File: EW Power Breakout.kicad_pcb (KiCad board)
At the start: 2 copper layers, 46.2 x 38.1 mm, 15 parts, among them J1 CONN_02X08, J2 JACK_2P, J3 JACK_2P, J4 JACK_2P, J5 JACK_2P, J6 CONN_01X14, U1 LM7805

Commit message: Fixed IDC routing bug
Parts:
- moved J6 2.51 mm to (157.0, 109.2)
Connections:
- D1 pad 2: Net-(D1-Pad2) -> /+12VI
- D2 pad 1: Net-(D2-Pad1) -> /-12VI
- J1 pad 1: Net-(J1-Pad1) -> /-12VI
- J1 pad 10: GND -> /+12VI
- J1 pad 12: GND -> Net-(J1-Pad12)
- J1 pad 13: Net-(J1-Pad13) -> /CV
- J1 pad 14: GND -> /CV
- J1 pad 15: Net-(J1-Pad15) -> /GATE
- J1 pad 16: Net-(D2-Pad1) -> /GATE
- J1 pad 2: /GATE -> /-12VI
- J1 pad 3: Net-(J1-Pad3) -> GND
- J1 pad 4: /CV -> GND
- J1 pad 5: Net-(J1-Pad5) -> GND
- J1 pad 6: Net-(J1-Pad6) -> GND
- J1 pad 7: Net-(J1-Pad7) -> GND
- J1 pad 8: Net-(D1-Pad2) -> GND
- J1 pad 9: Net-(J1-Pad9) -> /+12VI
- U1 pad 1: (no net) -> /+12V
- U1 pad 2: (no net) -> GND
- U1 pad 3: (no net) -> /+5V
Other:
- board size 46.2 x 38.1 mm -> 48.3 x 38.1 mm
- board text added: "+12V"
- board text added: "+5V"
- board text added: "-12V"
- board text added: "CV"
- board text added: "GATE"
- board text added: "GND"
- board text added: "J1"
- board text added: "J1SW"
- board text added: "J2"
- board text added: "J2SW"
- board text added: "J3"
- board text added: "J3SW"
- board text added: "J4"
- board text added: "J4SW"

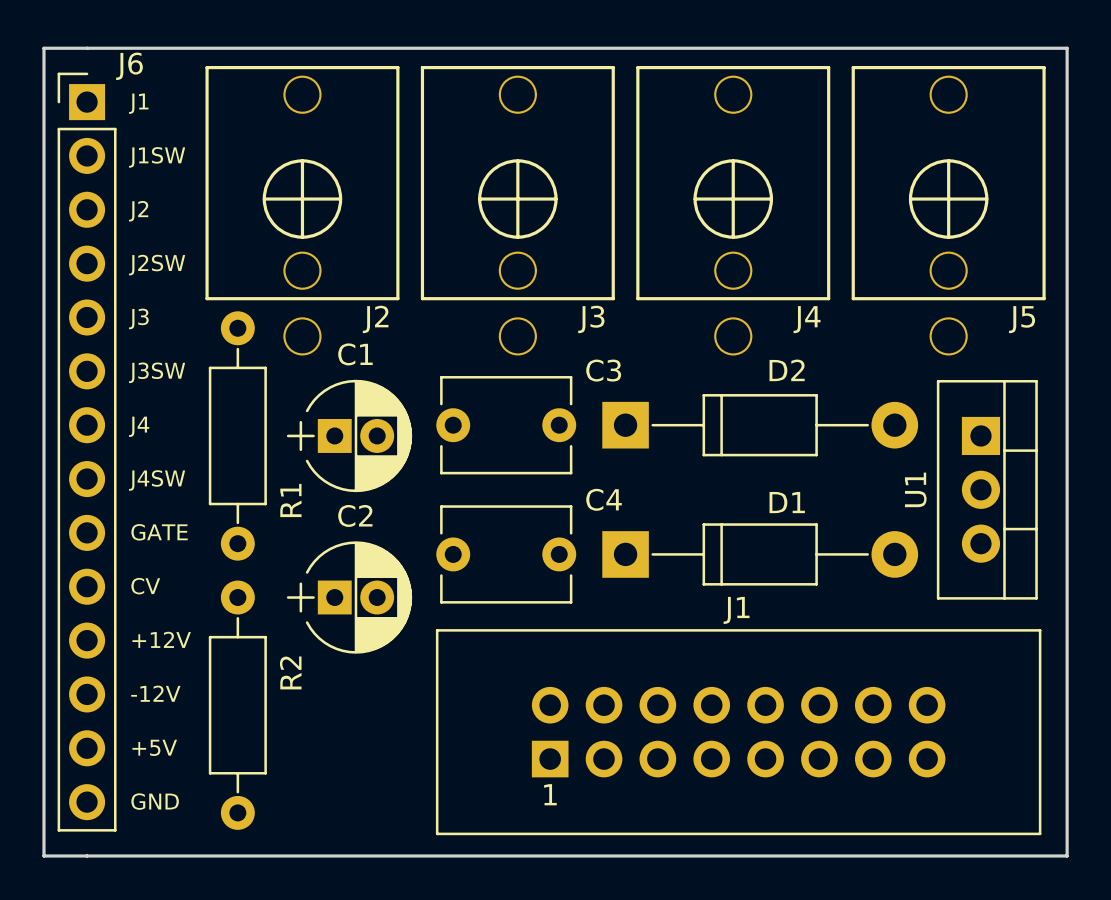
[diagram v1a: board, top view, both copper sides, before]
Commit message: Drills in PJ301M-12 jacks
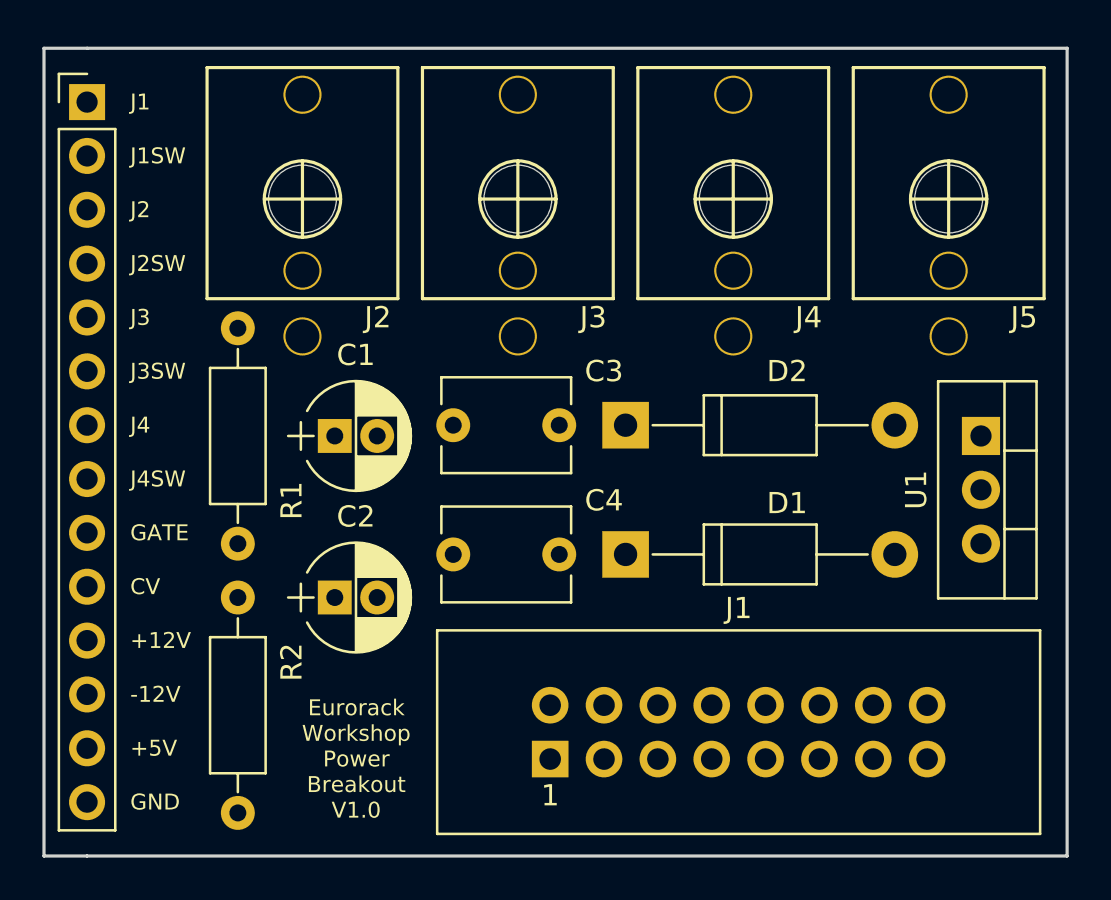
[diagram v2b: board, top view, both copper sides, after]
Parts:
- J2, J3, J4, J5: footprint Eurocad:PJ301M-12 -> lib:PJ301M-12
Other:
- board text added: ""I have nothing to say and I'm saying it""
- board text added: "- John Cage"
- board text added: "Eurorack Workshop Power Breakout V1.0"

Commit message: Design change. Connector to the left
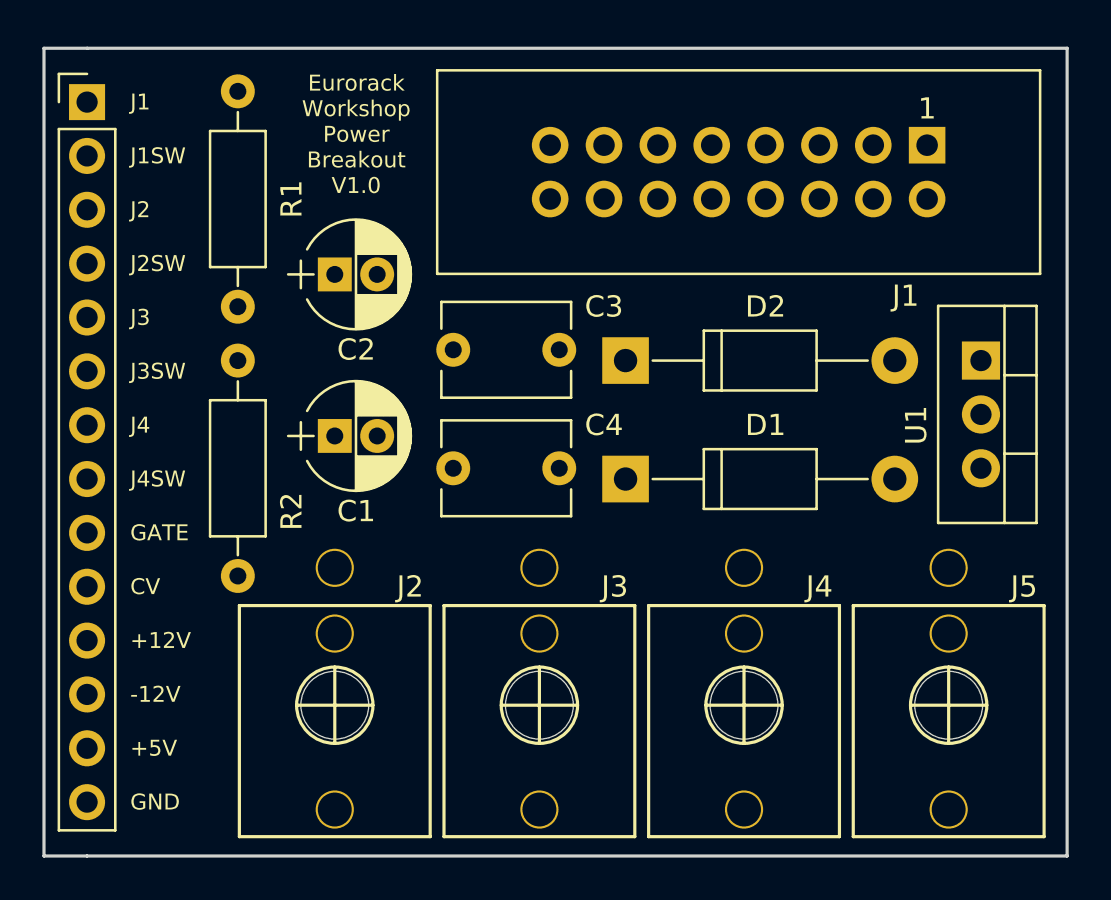
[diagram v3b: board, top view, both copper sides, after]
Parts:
- moved J1 34.0 mm to (196.6, 111.3), turned to 180 degrees
- moved J2 23.9 mm to (168.7, 137.7), turned to 180 degrees
- moved J3 23.9 mm to (178.3, 137.7), turned to 180 degrees
- moved J4 23.9 mm to (188.0, 137.7), turned to 180 degrees
- moved J5 23.9 mm to (197.6, 137.7), turned to 180 degrees
- moved C2 15.2 mm to (168.7, 117.3)
- moved R1 11.2 mm to (164.1, 118.9)
- moved R2 11.2 mm to (164.1, 131.6)
- moved C4 4.06 mm to (174.2, 126.5)
- moved D1 3.56 mm to (182.4, 127.0)
- moved C3 3.56 mm to (174.2, 120.9)
- moved U1 3.56 mm to (199.1, 121.4)
- moved D2 3.05 mm to (182.4, 121.4)
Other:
- net class Power added: clearance 0.3, trace_width 0.4, via_dia 0.7, via_drill 0.5

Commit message: Wiring PCB
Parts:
- moved J6 33.0 mm to (157.0, 142.2), turned to 180 degrees
- moved D1 13.9 mm to (195.1, 121.4), turned to 180 degrees
- moved D2 13.9 mm to (195.1, 127.0), turned to 180 degrees
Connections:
- J2 pad 1: /J1 -> GND
- J2 pad 3: GND -> /J1
- J3 pad 1: /J2 -> GND
- J3 pad 3: GND -> /J2
- J4 pad 1: /J3 -> GND
- J4 pad 3: GND -> /J3
- J5 pad 1: /J4 -> GND
- J5 pad 3: GND -> /J4
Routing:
- net GND: track 0.00 -> 184.5 mm
- net /+5V: track 0.00 -> 56.4 mm, vias 0 -> 1
- net /+12V: track 0.00 -> 52.8 mm, vias 0 -> 2
- net Net-(D1-Pad1): track 0.00 -> 48.7 mm, vias 0 -> 1
- net /J4: track 0.00 -> 48.3 mm
- net /J4SW: track 0.00 -> 44.7 mm
- net /GATE: track 0.00 -> 42.3 mm
- net /CV: track 0.00 -> 42.2 mm, vias 0 -> 1
- net /J3: track 0.00 -> 35.3 mm
- net /-12V: track 0.00 -> 34.1 mm, vias 0 -> 2
- net /J3SW: track 0.00 -> 33.8 mm
- net /J2: track 0.00 -> 23.6 mm
- net Net-(D2-Pad2): track 0.00 -> 23.1 mm
- net /J2SW: track 0.00 -> 22.9 mm
- net /-12VI: track 0.00 -> 17.2 mm
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
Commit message: GND copper fill
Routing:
- net GND: track 184.5 -> 141.7 mm
- net /+12V: track 52.8 -> 50.8 mm, vias 2 -> 4
- net /J3SW: track 33.8 -> 35.2 mm, vias 0 -> 2
- net /J2SW: track 22.9 -> 24.2 mm, vias 0 -> 2
- net Net-(D2-Pad2): track 23.1 -> 22.5 mm
- net /J4SW: track 44.7 -> 45.2 mm, vias 0 -> 2
- net /J1SW: vias 0 -> 2
- added copper zone on B.Cu, net GND
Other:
- board text added: "Eurorack Workshop Power Breakout v0.9"
- board text removed: "Eurorack Workshop Power Breakout V1.0"
